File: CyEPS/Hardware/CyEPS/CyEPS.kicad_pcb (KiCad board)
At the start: 2 copper layers, 101.6 x 76.2 mm, 96 parts, among them J1 Conn_01x04_Female, J2 Conn_01x04_Female, Q1 Si4931DY, Q2 Si4931DY, Q3 DMG2305UX, Q4 DMG2305UX, Q5 DMG2305UX, Q6 Si4931DY, U1 TPS61230DRC, U2 TPS61230DRC, U3 LTC4417HGN, U4 ADC128D818CIMTX_NOPB, U5 LM1117-3.3, U6 LM1117-3.3

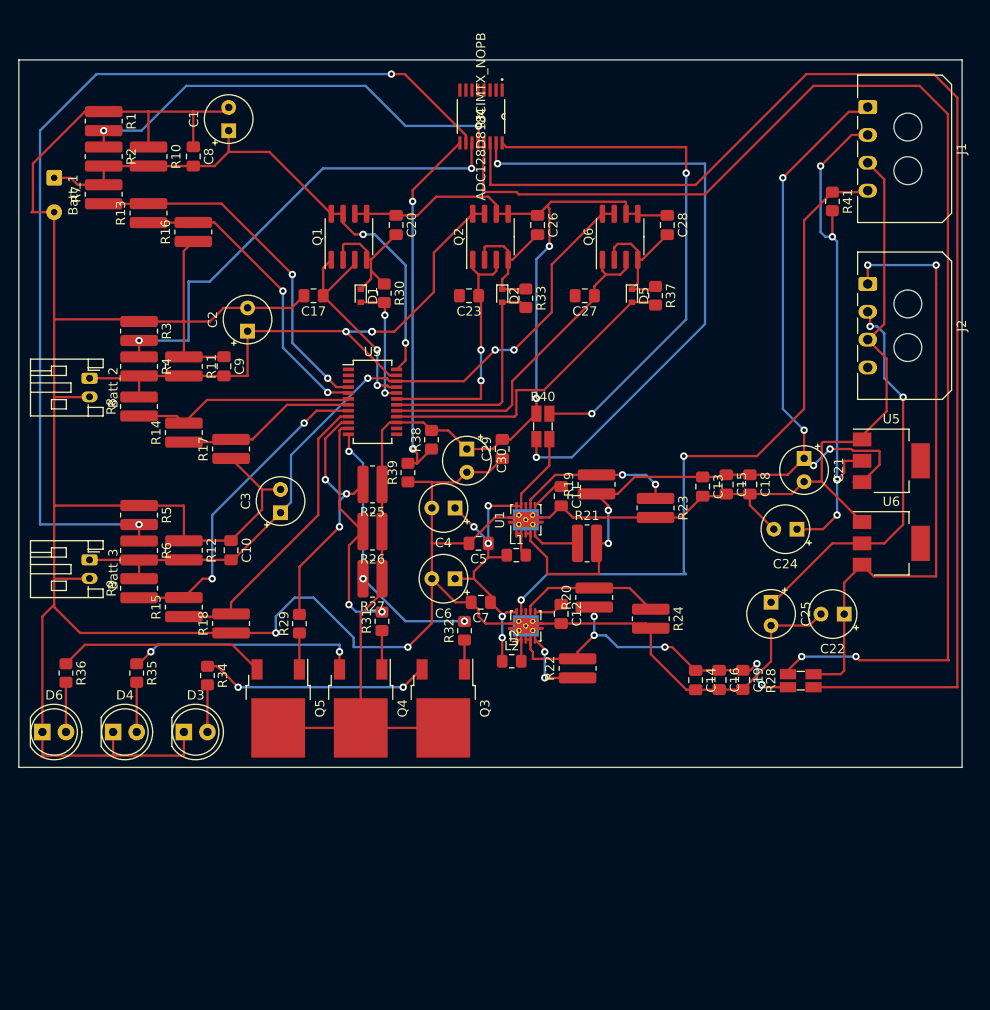
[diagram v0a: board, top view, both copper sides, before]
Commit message: Made some small changes based on Plewa's initial thoughts on the layout
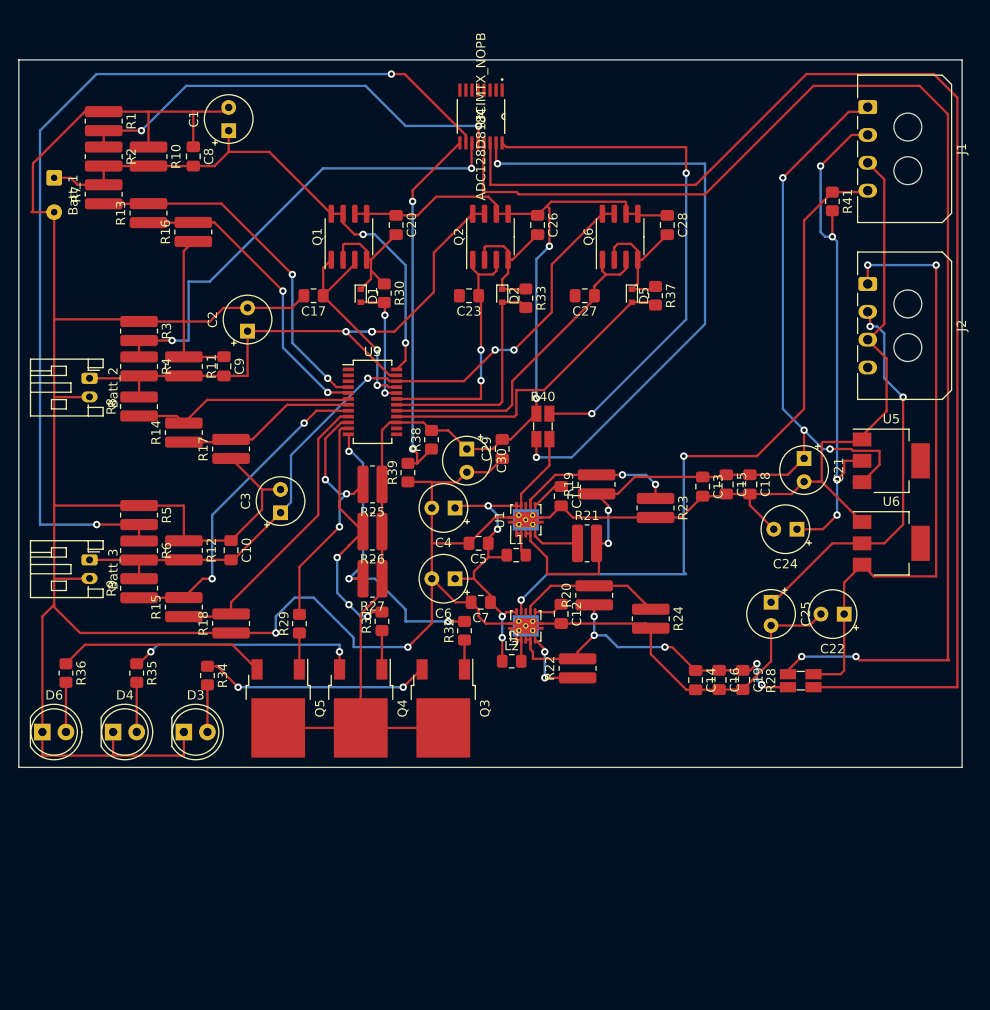
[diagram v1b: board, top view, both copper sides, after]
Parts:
- moved R20 0.24 mm to (74.7, 70.4)
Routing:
- net Net-(R27-Pad2): track 29.2 -> 33.6 mm
- net Net-(R26-Pad2): track 25.4 -> 26.8 mm, vias 2 -> 3
- net VSelect: track 42.0 -> 41.2 mm, vias 5 -> 4
- net Primary5V: track 103.4 -> 103.5 mm, vias 6 -> 5

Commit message: Power traces redone in .4mm width (max that would fit voltage select chip pads)
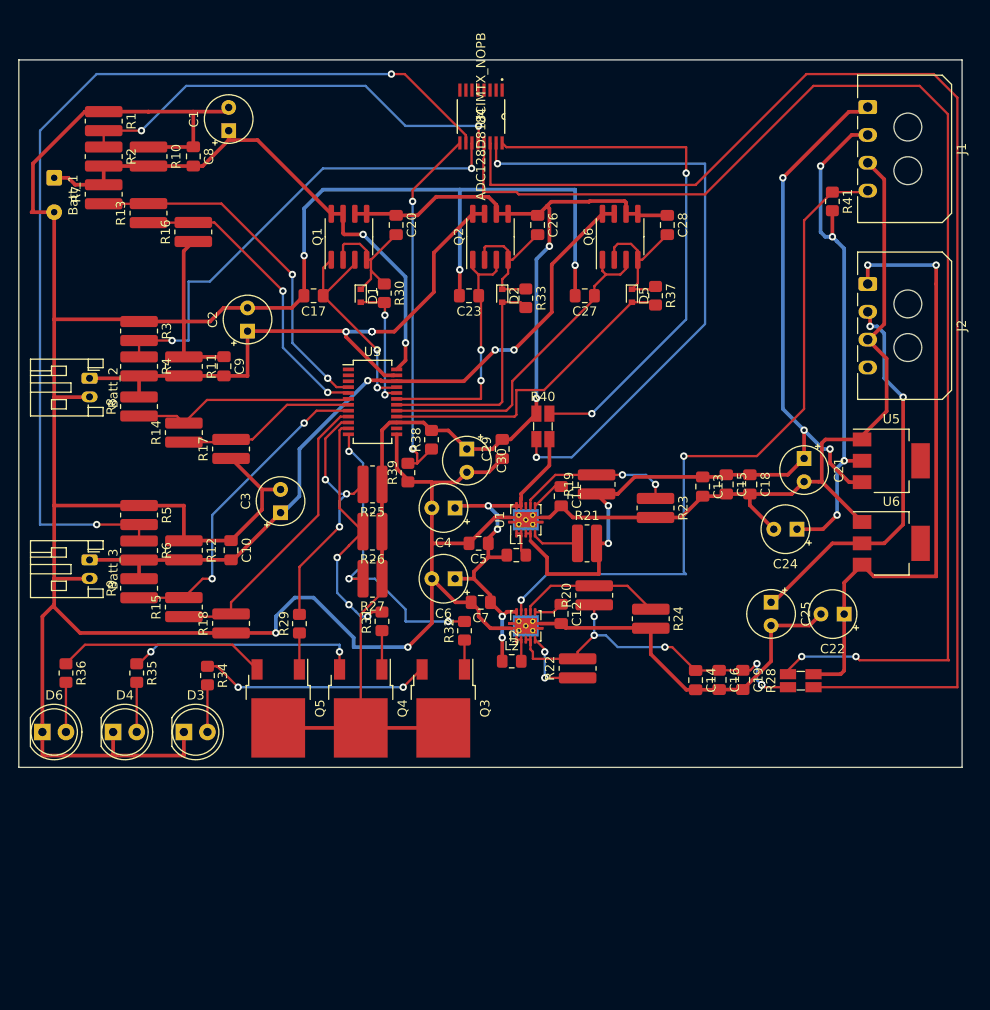
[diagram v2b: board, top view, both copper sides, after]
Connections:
- U3 pad 13: Net-(U3-Pad13) -> GND
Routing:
- net GND: track 430.3 -> 499.6 mm, vias 2 -> 5
- net Primary5V: track 103.5 -> 98.8 mm
- net Primary3V3: track 57.3 -> 55.6 mm, vias 5 -> 4

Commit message: form factor changed to 10cm x 10cm among other changes after review
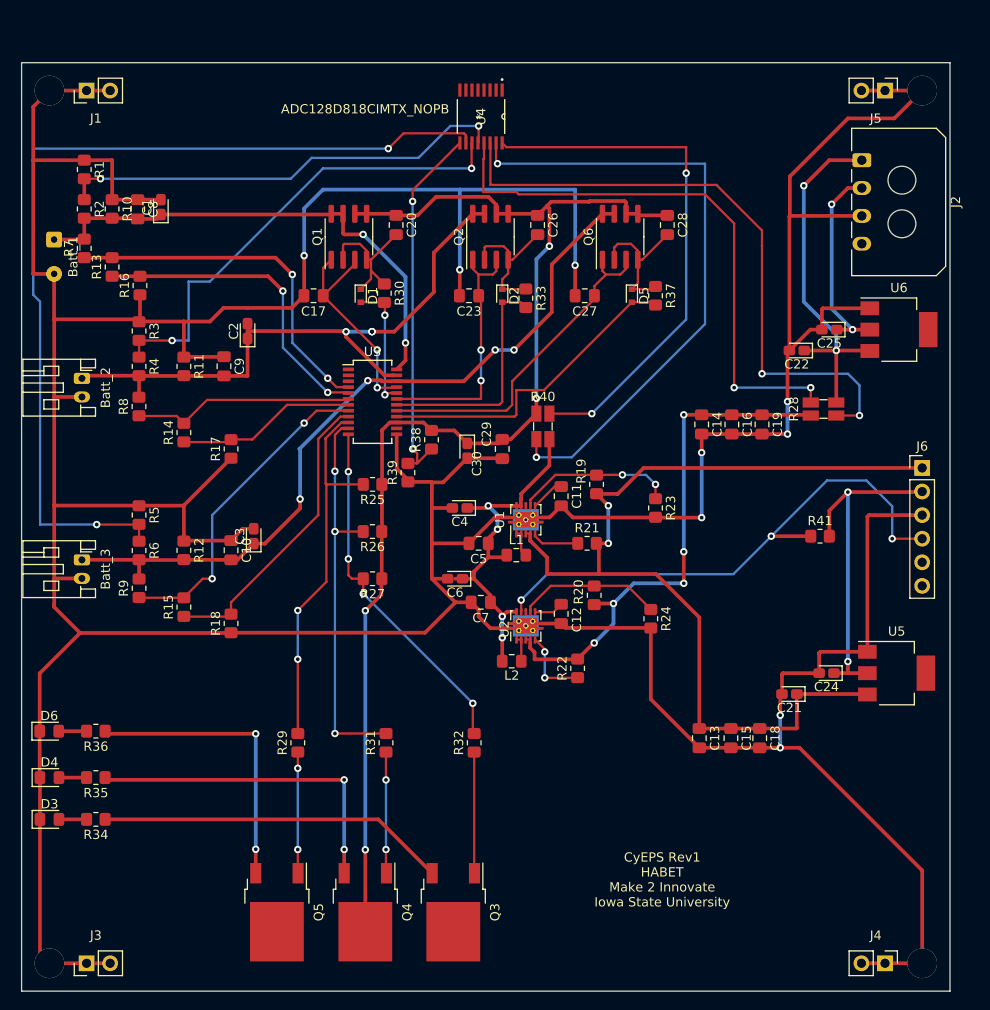
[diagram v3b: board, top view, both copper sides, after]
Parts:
- added J3: Conn_01x02_Female, Connector_PinHeader_2.54mm:PinHeader_1x02_P2.54mm_Vertical, F.Cu at (20.0, 110.0)
- added J4: Conn_01x02_Female, Connector_PinHeader_2.54mm:PinHeader_1x02_P2.54mm_Vertical, F.Cu at (106.0, 110.0)
- added J5: Conn_01x02_Female, Connector_PinHeader_2.54mm:PinHeader_1x02_P2.54mm_Vertical, F.Cu at (106.0, 16.0)
- added J6: Conn_01x06_Female, Connector_PinHeader_2.54mm:PinHeader_1x06_P2.54mm_Vertical, F.Cu at (110.0, 56.6)
- C1, C2, C21, C22, C24, C25, C3, C30, C4, C6: footprint Capacitor_THT:CP_Radial_Tantal_D5.0mm_P2.50mm -> Capacitor_Tantalum_SMD:CP_EIA-1608-08_AVX-J_Pad1.25x1.05mm_HandSolder
- D3, D4, D6: footprint LED_THT:LED_D5.0mm -> LED_SMD:LED_0805_2012Metric_Pad1.15x1.40mm_HandSolder
- J1: value Conn_01x04_Female -> Conn_01x02_Female; footprint Connector_Molex:Molex_Micro-Fit_3.0_43650-0400_1x04_P3.00mm_Horizontal -> Connector_PinHeader_2.54mm:PinHeader_1x02_P2.54mm_Vertical
- R1, R10, R11, R12, R13, R14, R15, R16, R17, R18, R19, R2, R20, R21, R22, R23, R24, R25, R26, R27, R3, R4, R5, R6, R7, R8, R9: footprint Resistor_SMD:R_0815_2038Metric_Pad1.20x4.05mm_HandSolder -> Resistor_SMD:R_0805_2012Metric_Pad1.20x1.40mm_HandSolder
- moved J1 84.2 mm to (20.0, 16.0), turned to 90 degrees
- moved R41 36.1 mm to (99.0, 64.0), turned to 0 degrees
- moved C25 30.0 mm to (100.0, 41.8), turned to 180 degrees
- moved R28 29.4 mm to (99.4, 50.3)
- moved C22 28.8 mm to (96.5, 44.0)
- moved C19 27.6 mm to (92.8, 52.0)
- moved C16 27.6 mm to (89.5, 52.0)
- moved C14 27.5 mm to (86.2, 52.0)
- moved C18 27.4 mm to (92.5, 85.8)
- moved C15 27.3 mm to (89.4, 85.8)
- moved C13 27.1 mm to (86.0, 85.8)
- moved C21 25.4 mm to (95.7, 81.0), turned to 180 degrees
- moved U6 23.0 mm to (107.5, 41.8)
- moved U5 22.9 mm to (107.2, 78.8)
- moved Q3 22.0 mm to (59.5, 104.5)
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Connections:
- J1 pad 1: Primary5V -> GND
- J1 pad 2: Primary3V3 -> GND
- J2 pad 4: Net-(J2-Pad4) -> (no net)
- U3 pad 1: Net-(U3-Pad1) -> (no net)
- U3 pad 14: Net-(U3-Pad14) -> (no net)
- U3 pad 2: Net-(U3-Pad2) -> (no net)
- U3 pad 3: Net-(U3-Pad3) -> (no net)
- U4 pad 1: Net-(U4-Pad1) -> (no net)
- U4 pad 2: Net-(U4-Pad2) -> (no net)
- U4 pad 3: Net-(U4-Pad3) -> (no net)
- U4 pad 4: Net-(U4-Pad4) -> (no net)
- U4 pad 5: Net-(U4-Pad5) -> (no net)
- U4 pad 6: Net-(U4-Pad6) -> (no net)
- U4 pad 7: Net-(U4-Pad7) -> (no net)
- U4 pad 8: Net-(U4-Pad8) -> (no net)
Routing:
- net GND: track 499.6 -> 587.7 mm, vias 5 -> 13
- net IN3: track 139.0 -> 61.3 mm
- net IN2: track 139.8 -> 68.1 mm, vias 0 -> 2
- net Payload5V: track 67.1 -> 39.3 mm
- net Payload3V3: track 42.6 -> 22.0 mm
- net Primary3V3: track 55.6 -> 36.7 mm, vias 4 -> 2
- net Net-(C14-Pad1): track 39.2 -> 57.3 mm, vias 6 -> 5
- net PayloadEnable: track 76.6 -> 58.7 mm, vias 2 -> 3
- net Net-(R26-Pad2): track 26.8 -> 42.4 mm
- net Net-(Q3-Pad3): track 24.9 -> 37.6 mm, vias 2 -> 0
- net Net-(R25-Pad2): track 27.8 -> 40.3 mm, vias 3 -> 2
- net Net-(Q4-Pad3): track 25.4 -> 35.9 mm
- net Net-(Q3-Pad1): track 3.17 -> 13.1 mm
- net Net-(Q5-Pad1): track 3.93 -> 13.1 mm, vias 0 -> 2
- net Net-(Q4-Pad1): track 4.18 -> 13.1 mm, vias 0 -> 2
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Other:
- board size 101.6 x 76.2 mm -> 100 x 100 mm
- board text added: "CyEPS Rev1 HABET Make 2 Innovate Iowa State University"
